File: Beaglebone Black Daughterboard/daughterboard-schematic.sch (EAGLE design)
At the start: 7 parts

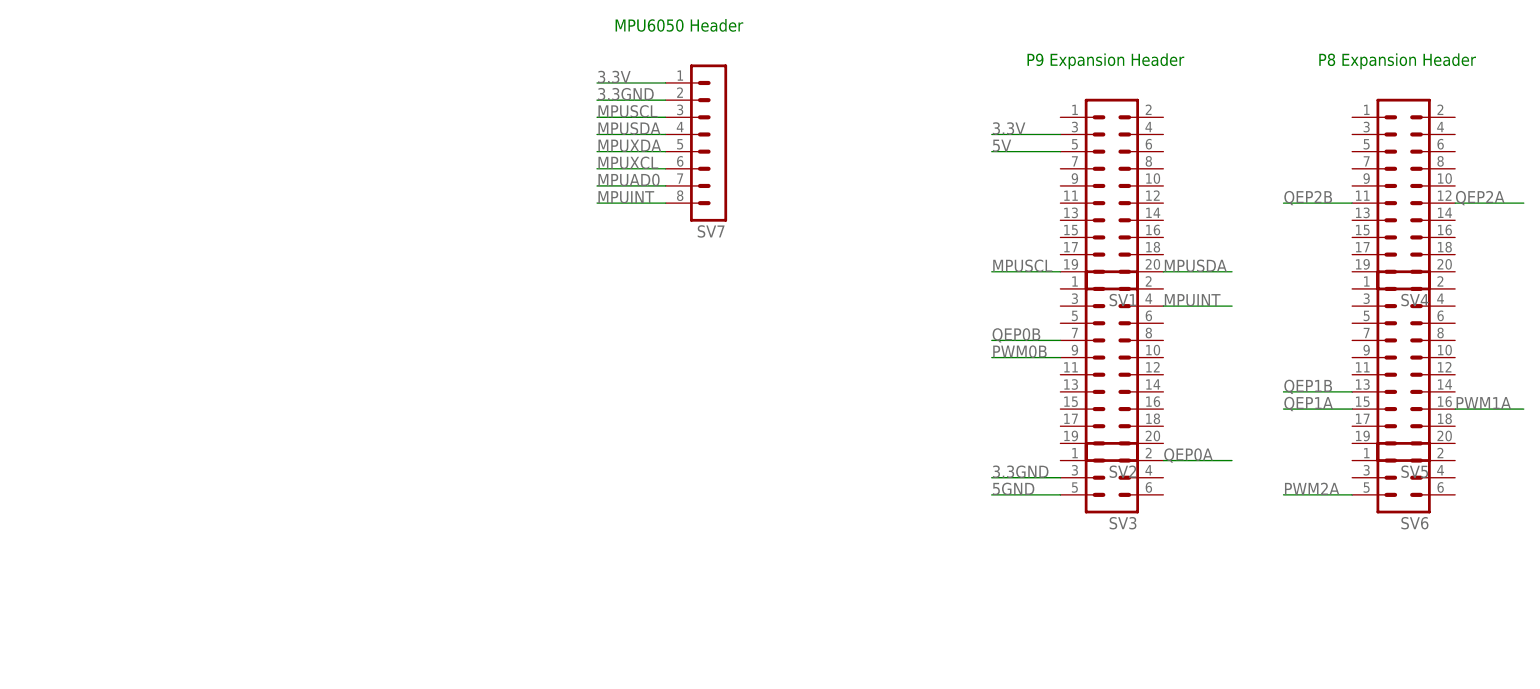
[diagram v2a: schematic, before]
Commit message: Add 40109 and it's library and wire up its ports for one qep
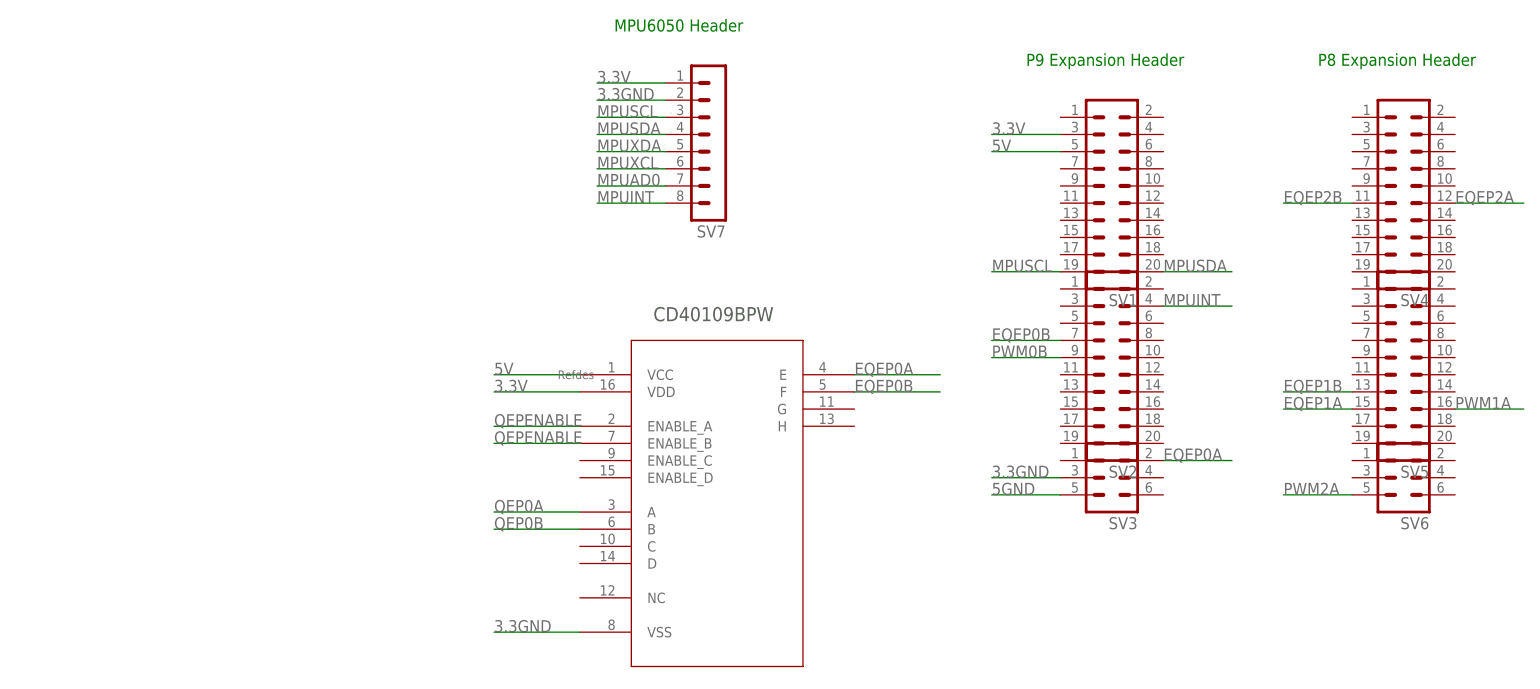
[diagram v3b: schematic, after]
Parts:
- added U1: CD40109BPW, Texas Instruments_By_element14_Batch_1:CD40109BPW
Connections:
- net QEP1A renamed EQEP1A
- net QEP1B renamed EQEP1B
- net QEP2A renamed EQEP2A
- net QEP2B renamed EQEP2B
- new net EQEP0A: SV3.2, U1.E
- new net EQEP0B: SV2.7, U1.F
- new net QEPENABLE: U1.ENABLE_A, U1.ENABLE_B
- net 3.3GND: now also U1.VSS
- net 3.3V: now also U1.VDD
- net 5V: now also U1.VCC
- net QEP0A: now also U1.A; no longer SV3.2
- net QEP0B: now also U1.B; no longer SV2.7
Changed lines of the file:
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@@
 <part name="SV6" library="con-lstb" deviceset="MA03-2" device=""/>
 <part name="SV7" library="con-lstb" deviceset="MA08-1" device=""/>
+<part name="U1" library="Texas Instruments_By_element14_Batch_1" deviceset="CD40109BPW" device=""/>
 </parts>
 <sheets>
@@
 <instance part="SV6" gate="1" x="190.5" y="43.18" rot="R180"/>
 <instance part="SV7" gate="1" x="88.9" y="93.98" rot="R180"/>
+<instance part="U1" gate="A" x="68.58" y="58.42"/>
 </instances>
 <busses>
@@
 <label x="71.12" y="101.6" size="1.778" layer="95"/>
 </segment>
+<segment>
+<pinref part="U1" gate="A" pin="VDD"/>
+<wire x1="68.58" y1="55.88" x2="55.88" y2="55.88" width="0.1524" layer="91"/>
+<label x="55.88" y="55.88" size="1.778" layer="95"/>
+</segment>
 </net>
 <net name="5V" class="0">
@@
 <label x="129.54" y="91.44" size="1.778" layer="95"/>
 </segment>
+<segment>
+<pinref part="U1" gate="A" pin="VCC"/>
+<wire x1="68.58" y1="58.42" x2="55.88" y2="58.42" width="0.1524" layer="91"/>
+<label x="55.88" y="58.42" size="1.778" layer="95"/>
+</segment>
 </net>
 <net name="PWM0B" class="0">
@@
 <label x="71.12" y="99.06" size="1.778" layer="95"/>
 </segment>
+<segment>
+<pinref part="U1" gate="A" pin="VSS"/>
+<wire x1="68.58" y1="20.32" x2="55.88" y2="20.32" width="0.1524" layer="91"/>
+<label x="55.88" y="20.32" size="1.778" layer="95"/>
+</segment>
 </net>
 <net name="5GND" class="0">
@@
 </segment>
 </net>
+<net name="EQEP1A" class="0">
+<segment>
+<pinref part="SV5" gate="1" pin="15"/>
+<wire x1="182.88" y1="53.34" x2="172.72" y2="53.34" width="0.1524" layer="91"/>
+<label x="172.72" y="53.34" size="1.778" layer="95"/>
+</segment>
+</net>
+<net name="EQEP1B" class="0">
+<segment>
+<pinref part="SV5" gate="1" pin="13"/>
+<wire x1="182.88" y1="55.88" x2="172.72" y2="55.88" width="0.1524" layer="91"/>
+<label x="172.72" y="55.88" size="1.778" layer="95"/>
+</segment>
+</net>
+<net name="EQEP2A" class="0">
+<segment>
+<pinref part="SV4" gate="1" pin="12"/>
+<wire x1="198.12" y1="83.82" x2="208.28" y2="83.82" width="0.1524" layer="91"/>
+<label x="198.12" y="83.82" size="1.778" layer="95"/>
+</segment>
+</net>
+<net name="EQEP2B" class="0">
+<segment>
+<pinref part="SV4" gate="1" pin="11"/>
+<wire x1="182.88" y1="83.82" x2="172.72" y2="83.82" width="0.1524" layer="91"/>
+<label x="172.72" y="83.82" size="1.778" layer="95"/>
+</segment>
+</net>
+<net name="MPUSCL" class="0">
+<segment>
+<pinref part="SV1" gate="1" pin="19"/>
+<wire x1="139.7" y1="73.66" x2="129.54" y2="73.66" width="0.1524" layer="91"/>
+<label x="129.54" y="73.66" size="1.778" layer="95"/>
+</segment>
+<segment>
+<pinref part="SV7" gate="1" pin="3"/>
+<wire x1="81.28" y1="96.52" x2="71.12" y2="96.52" width="0.1524" layer="91"/>
+<label x="71.12" y="96.52" size="1.778" layer="95"/>
+</segment>
+</net>
+<net name="MPUSDA" class="0">
+<segment>
+<pinref part="SV1" gate="1" pin="20"/>
+<wire x1="154.94" y1="73.66" x2="165.1" y2="73.66" width="0.1524" layer="91"/>
+<label x="154.94" y="73.66" size="1.778" layer="95"/>
+</segment>
+<segment>
+<pinref part="SV7" gate="1" pin="4"/>
+<wire x1="81.28" y1="93.98" x2="71.12" y2="93.98" width="0.1524" layer="91"/>
+<label x="71.12" y="93.98" size="1.778" layer="95"/>
+</segment>
+</net>
+<net name="MPUINT" class="0">
+<segment>
+<pinref part="SV2" gate="1" pin="4"/>
+<wire x1="154.94" y1="68.58" x2="165.1" y2="68.58" width="0.1524" layer="91"/>
+<label x="154.94" y="68.58" size="1.778" layer="95"/>
+</segment>
+<segment>
+<pinref part="SV7" gate="1" pin="8"/>
+<wire x1="81.28" y1="83.82" x2="71.12" y2="83.82" width="0.1524" layer="91"/>
+<label x="71.12" y="83.82" size="1.778" layer="95"/>
+</segment>
+</net>
+<net name="MPUXDA" class="0">
+<segment>
+<pinref part="SV7" gate="1" pin="5"/>
+<wire x1="81.28" y1="91.44" x2="71.12" y2="91.44" width="0.1524" layer="91"/>
+<label x="71.12" y="91.44" size="1.778" layer="95"/>
+</segment>
+</net>
+<net name="MPUXCL" class="0">
+<segment>
+<pinref part="SV7" gate="1" pin="6"/>
+<wire x1="81.28" y1="88.9" x2="71.12" y2="88.9" width="0.1524" layer="91"/>
+<label x="71.12" y="88.9" size="1.778" layer="95"/>
+</segment>
+</net>
+<net name="MPUAD0" class="0">
+<segment>
+<pinref part="SV7" gate="1" pin="7"/>
+<wire x1="81.28" y1="86.36" x2="71.12" y2="86.36" width="0.1524" layer="91"/>
+<label x="71.12" y="86.36" size="1.778" layer="95"/>
+</segment>
+</net>
+<net name="QEPENABLE" class="0">
+<segment>
+<pinref part="U1" gate="A" pin="ENABLE_A"/>
+<wire x1="68.58" y1="50.8" x2="55.88" y2="50.8" width="0.1524" layer="91"/>
+<label x="55.88" y="50.8" size="1.778" layer="95"/>
+</segment>
+<segment>
+<pinref part="U1" gate="A" pin="ENABLE_B"/>
+<wire x1="68.58" y1="48.26" x2="55.88" y2="48.26" width="0.1524" layer="91"/>
+<label x="55.88" y="48.26" size="1.778" layer="95"/>
+</segment>
+</net>
 <net name="QEP0A" class="0">
+<segment>
+<pinref part="U1" gate="A" pin="A"/>
+<wire x1="68.58" y1="38.1" x2="55.88" y2="38.1" width="0.1524" layer="91"/>
+<label x="55.88" y="38.1" size="1.778" layer="95"/>
+</segment>
+</net>
+<net name="QEP0B" class="0">
+<segment>
+<pinref part="U1" gate="A" pin="B"/>
+<wire x1="68.58" y1="35.56" x2="55.88" y2="35.56" width="0.1524" layer="91"/>
+<label x="55.88" y="35.56" size="1.778" layer="95"/>
+</segment>
+</net>
+<net name="EQEP0B" class="0">
+<segment>
+<pinref part="SV2" gate="1" pin="7"/>
+<wire x1="139.7" y1="63.5" x2="129.54" y2="63.5" width="0.1524" layer="91"/>
+<label x="129.54" y="63.5" size="1.778" layer="95"/>
+</segment>
+<segment>
+<pinref part="U1" gate="A" pin="F"/>
+<wire x1="109.22" y1="55.88" x2="121.92" y2="55.88" width="0.1524" layer="91"/>
+<label x="109.22" y="55.88" size="1.778" layer="95"/>
+</segment>
+</net>
+<net name="EQEP0A" class="0">
 <segment>
 <pinref part="SV3" gate="1" pin="2"/>
@@
 <label x="154.94" y="45.72" size="1.778" layer="95"/>
 </segment>
-</net>
-<net name="QEP0B" class="0">
-<segment>
-<pinref part="SV2" gate="1" pin="7"/>
-<wire x1="139.7" y1="63.5" x2="129.54" y2="63.5" width="0.1524" layer="91"/>
-<label x="129.54" y="63.5" size="1.778" layer="95"/>
-</segment>
-</net>
-<net name="QEP1A" class="0">
-<segment>
-<pinref part="SV5" gate="1" pin="15"/>
-<wire x1="182.88" y1="53.34" x2="172.72" y2="53.34" width="0.1524" layer="91"/>
-<label x="172.72" y="53.34" size="1.778" layer="95"/>
-</segment>
-</net>
-<net name="QEP1B" class="0">
-<segment>
-<pinref part="SV5" gate="1" pin="13"/>
-<wire x1="182.88" y1="55.88" x2="172.72" y2="55.88" width="0.1524" layer="91"/>
-<label x="172.72" y="55.88" size="1.778" layer="95"/>
-</segment>
-</net>
-<net name="QEP2A" class="0">
-<segment>
-<pinref part="SV4" gate="1" pin="12"/>
-<wire x1="198.12" y1="83.82" x2="208.28" y2="83.82" width="0.1524" layer="91"/>
-<label x="198.12" y="83.82" size="1.778" layer="95"/>
-</segment>
-</net>
-<net name="QEP2B" class="0">
-<segment>
-<pinref part="SV4" gate="1" pin="11"/>
-<wire x1="182.88" y1="83.82" x2="172.72" y2="83.82" width="0.1524" layer="91"/>
-<label x="172.72" y="83.82" size="1.778" layer="95"/>
-</segment>
-</net>
-<net name="MPUSCL" class="0">
-<segment>
-<pinref part="SV1" gate="1" pin="19"/>
-<wire x1="139.7" y1="73.66" x2="129.54" y2="73.66" width="0.1524" layer="91"/>
-<label x="129.54" y="73.66" size="1.778" layer="95"/>
-</segment>
-<segment>
-<pinref part="SV7" gate="1" pin="3"/>
-<wire x1="81.28" y1="96.52" x2="71.12" y2="96.52" width="0.1524" layer="91"/>
-<label x="71.12" y="96.52" size="1.778" layer="95"/>
-</segment>
-</net>
-<net name="MPUSDA" class="0">
-<segment>
-<pinref part="SV1" gate="1" pin="20"/>
-<wire x1="154.94" y1="73.66" x2="165.1" y2="73.66" width="0.1524" layer="91"/>
-<label x="154.94" y="73.66" size="1.778" layer="95"/>
-</segment>
-<segment>
-<pinref part="SV7" gate="1" pin="4"/>
-<wire x1="81.28" y1="93.98" x2="71.12" y2="93.98" width="0.1524" layer="91"/>
-<label x="71.12" y="93.98" size="1.778" layer="95"/>
-</segment>
-</net>
-<net name="MPUINT" class="0">
-<segment>
-<pinref part="SV2" gate="1" pin="4"/>
-<wire x1="154.94" y1="68.58" x2="165.1" y2="68.58" width="0.1524" layer="91"/>
-<label x="154.94" y="68.58" size="1.778" layer="95"/>
-</segment>
-<segment>
-<pinref part="SV7" gate="1" pin="8"/>
-<wire x1="81.28" y1="83.82" x2="71.12" y2="83.82" width="0.1524" layer="91"/>
-<label x="71.12" y="83.82" size="1.778" layer="95"/>
-</segment>
-</net>
-<net name="MPUXDA" class="0">
-<segment>
-<pinref part="SV7" gate="1" pin="5"/>
-<wire x1="81.28" y1="91.44" x2="71.12" y2="91.44" width="0.1524" layer="91"/>
-<label x="71.12" y="91.44" size="1.778" layer="95"/>
-</segment>
-</net>
-<net name="MPUXCL" class="0">
-<segment>
-<pinref part="SV7" gate="1" pin="6"/>
-<wire x1="81.28" y1="88.9" x2="71.12" y2="88.9" width="0.1524" layer="91"/>
-<label x="71.12" y="88.9" size="1.778" layer="95"/>
-</segment>
-</net>
-<net name="MPUAD0" class="0">
-<segment>
-<pinref part="SV7" gate="1" pin="7"/>
-<wire x1="81.28" y1="86.36" x2="71.12" y2="86.36" width="0.1524" layer="91"/>
-<label x="71.12" y="86.36" size="1.778" layer="95"/>
-</segment>
-</net>
+<segment>
+<pinref part="U1" gate="A" pin="E"/>
+<wire x1="109.22" y1="58.42" x2="121.92" y2="58.42" width="0.1524" layer="91"/>
+<label x="109.22" y="58.42" size="1.778" layer="95"/>
+</segment>
+</net>

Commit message: Have only one ground and create second 40109
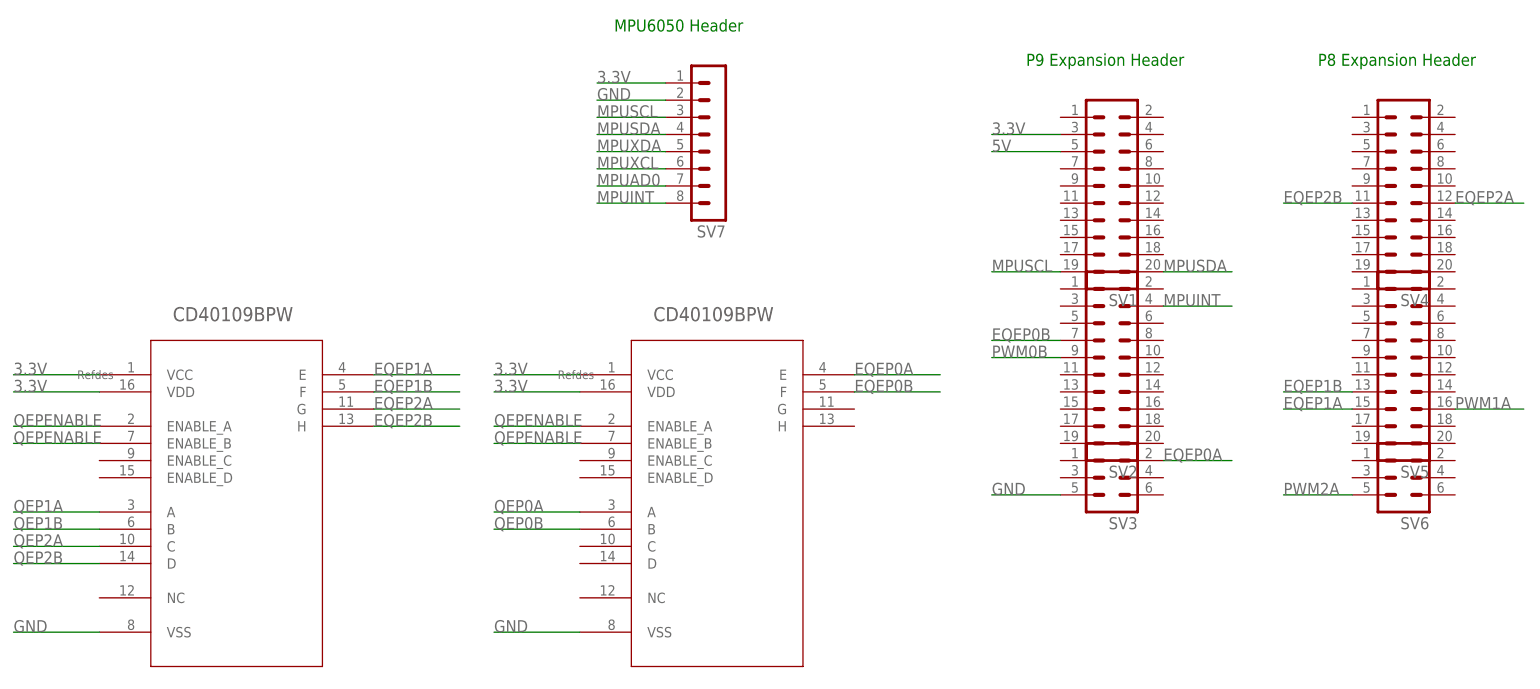
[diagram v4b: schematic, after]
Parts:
- added U2: CD40109BPW, Texas Instruments_By_element14_Batch_1:CD40109BPW
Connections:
- removed net 3.3GND: SV3.3, SV7.2, U1.VSS
- removed net 5GND: SV3.5
- new net GND: SV3.5, SV7.2, U1.VSS, U2.VSS
- new net QEP1A: U2.A
- new net QEP1B: U2.B
- new net QEP2A: U2.C
- new net QEP2B: U2.D
- net 3.3V: now also U1.VCC, U2.VCC, U2.VDD
- net 5V: no longer U1.VCC
- net EQEP1A: now also U2.E
- net EQEP1B: now also U2.F
- net EQEP2A: now also U2.G
- net EQEP2B: now also U2.H
- net QEPENABLE: now also U2.ENABLE_A, U2.ENABLE_B

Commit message: Put in qepenables
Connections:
- net QEPENABLE: now also U2.ENABLE_C, U2.ENABLE_D
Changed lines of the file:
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@@
 <label x="-15.24" y="48.26" size="1.778" layer="95"/>
+</segment>
+<segment>
+<pinref part="U2" gate="A" pin="ENABLE_C"/>
+<wire x1="-2.54" y1="45.72" x2="-15.24" y2="45.72" width="0.1524" layer="91"/>
+<label x="-15.24" y="45.72" size="1.778" layer="95"/>
+</segment>
+<segment>
+<pinref part="U2" gate="A" pin="ENABLE_D"/>
+<wire x1="-2.54" y1="43.18" x2="-15.24" y2="43.18" width="0.1524" layer="91"/>
+<label x="-15.24" y="43.18" size="1.778" layer="95"/>
 </segment>
 </net>

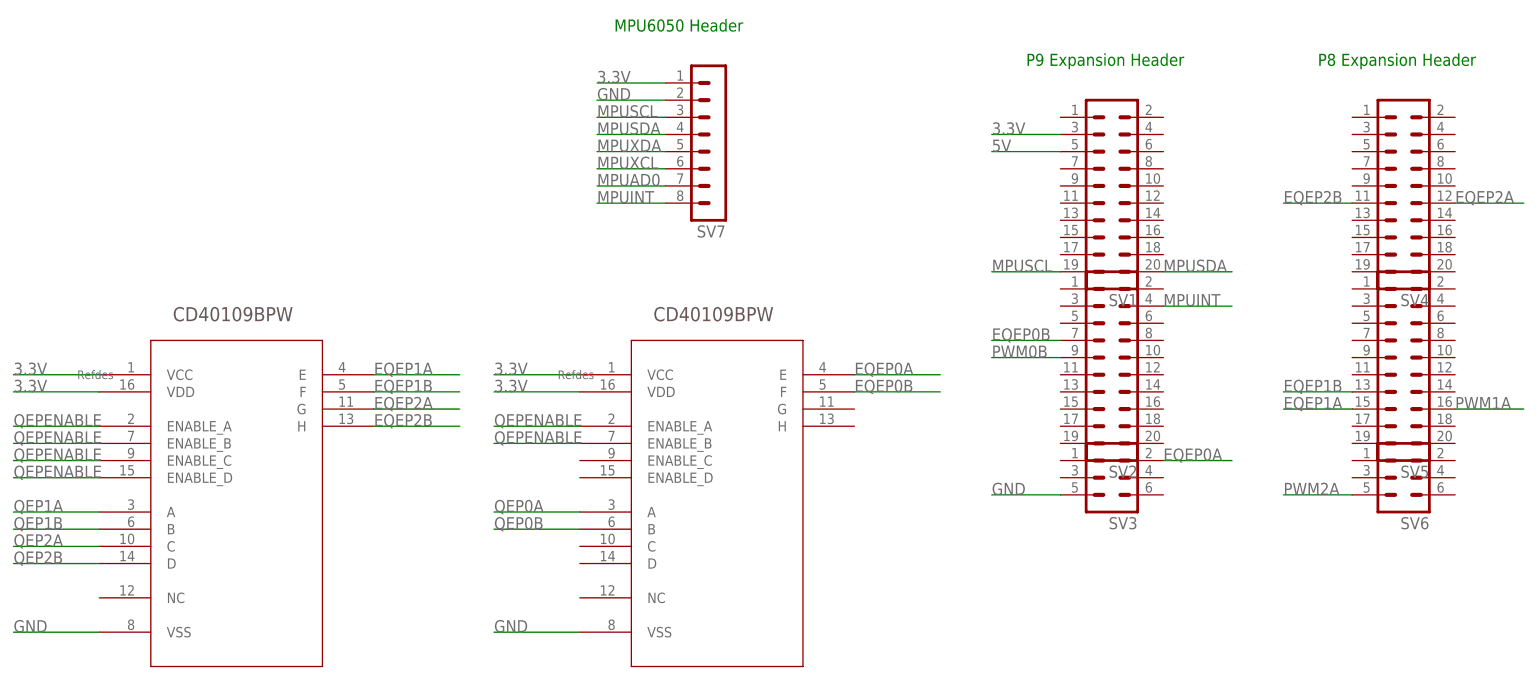
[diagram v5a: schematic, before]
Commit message: Replace 40109s with dip 16s
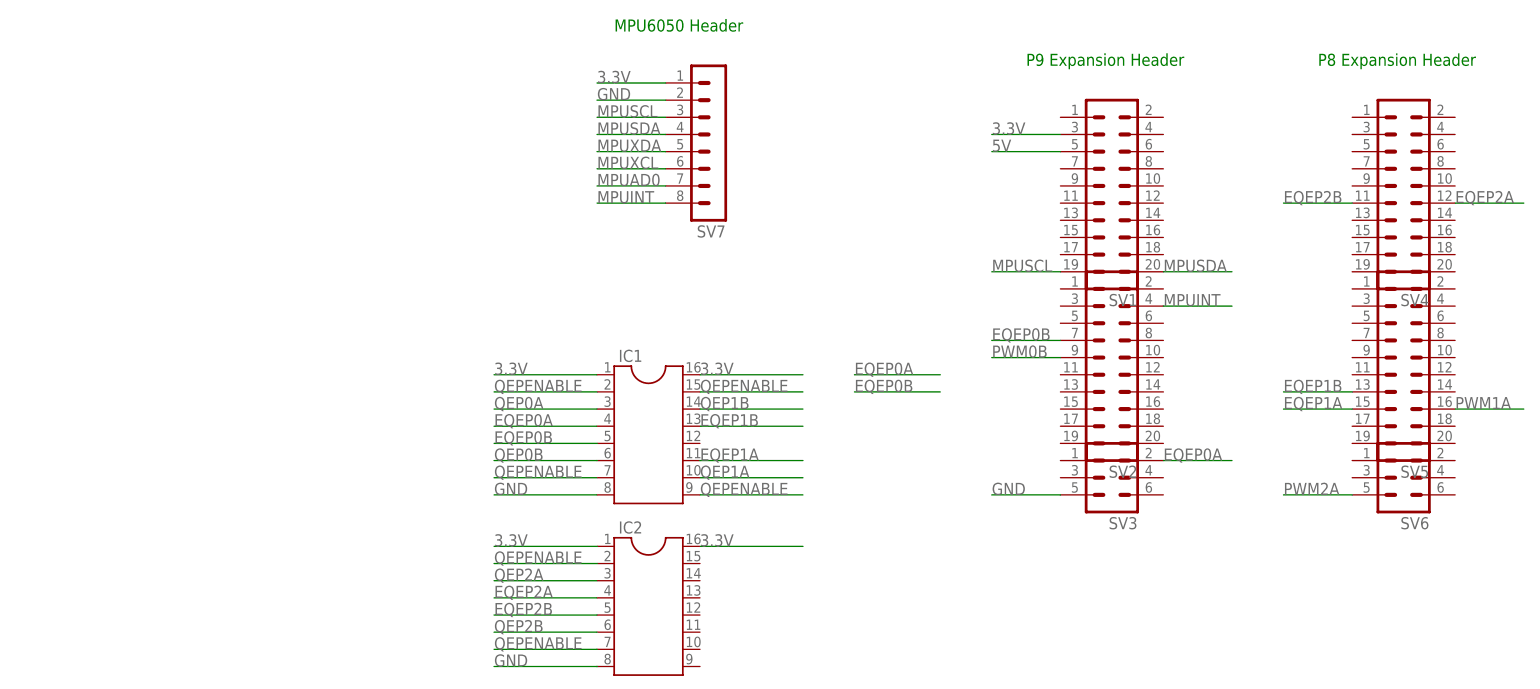
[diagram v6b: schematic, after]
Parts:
- removed U1, U2: CD40109BPW, Texas Instruments_By_element14_Batch_1:CD40109BPW
- added IC1, IC2: (no value), ic-package:DIL16
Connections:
- net 3.3V: now also IC1.1, IC1.16, IC2.1, IC2.16; no longer U1.VCC, U1.VDD, U2.VCC, U2.VDD
- net EQEP0A: now also IC1.4; no longer U1.E
- net EQEP0B: now also IC1.5; no longer U1.F
- net EQEP1A: now also IC1.11; no longer U2.E
- net EQEP1B: now also IC1.13; no longer U2.F
- net EQEP2A: now also IC2.4; no longer U2.G
- net EQEP2B: now also IC2.5; no longer U2.H
- net GND: now also IC1.8, IC2.8; no longer U1.VSS, U2.VSS
- net QEP0A: now also IC1.3; no longer U1.A
- net QEP0B: now also IC1.6; no longer U1.B
- net QEP1A: now also IC1.10; no longer U2.A
- net QEP1B: now also IC1.14; no longer U2.B
- net QEP2A: now also IC2.3; no longer U2.C
- net QEP2B: now also IC2.6; no longer U2.D
- net QEPENABLE: now also IC1.15, IC1.2, IC1.7, IC1.9, IC2.2, IC2.7; no longer U1.ENABLE_A, U1.ENABLE_B, U2.ENABLE_A, U2.ENABLE_B, U2.ENABLE_C, U2.ENABLE_D
